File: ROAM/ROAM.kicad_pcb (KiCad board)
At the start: 4 copper layers, 90 x 56.8 mm, 11 parts, among them J1 CommanderX16Expansion Alt, U1 SST39SF040 (ROM), U2 74HCT00, U3 74HCT138, U4 AS6C4008 (RAM)

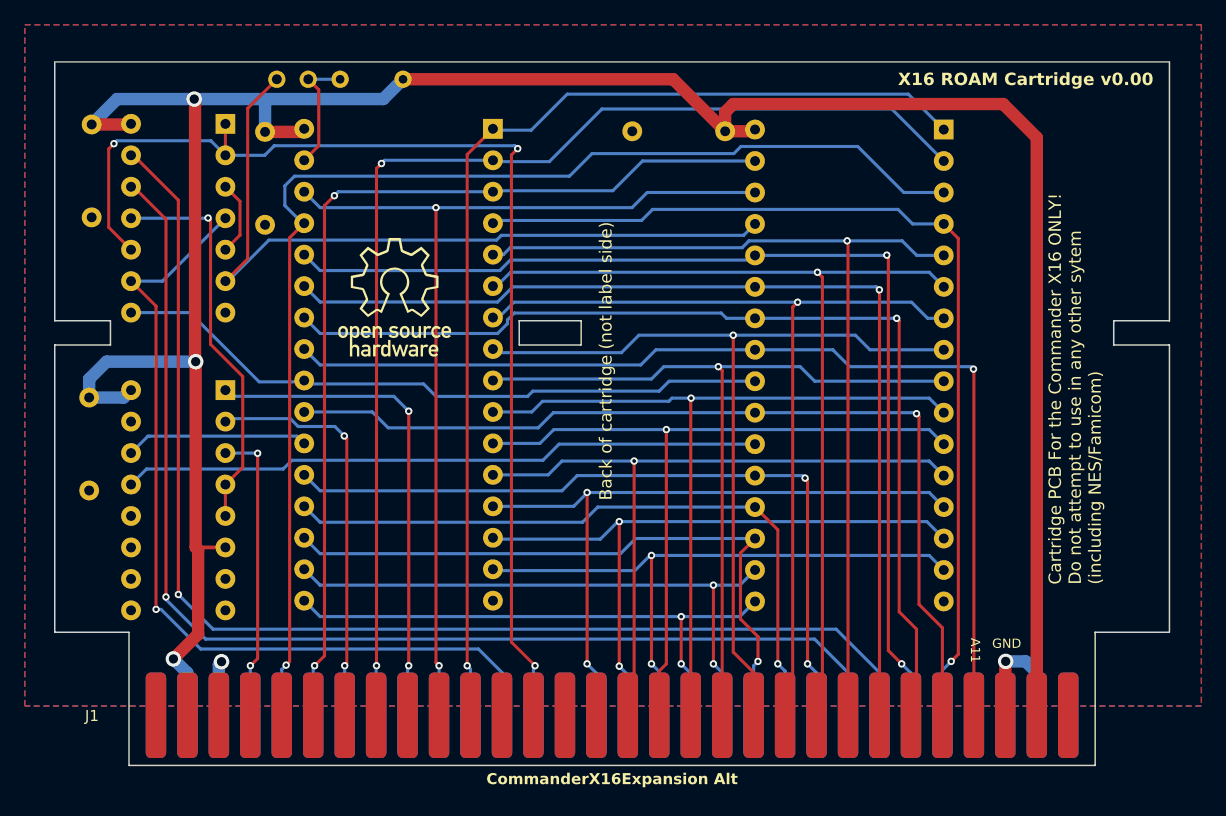
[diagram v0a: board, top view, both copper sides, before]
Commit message: Add NVRAM, add edge connector sym/fp to proj
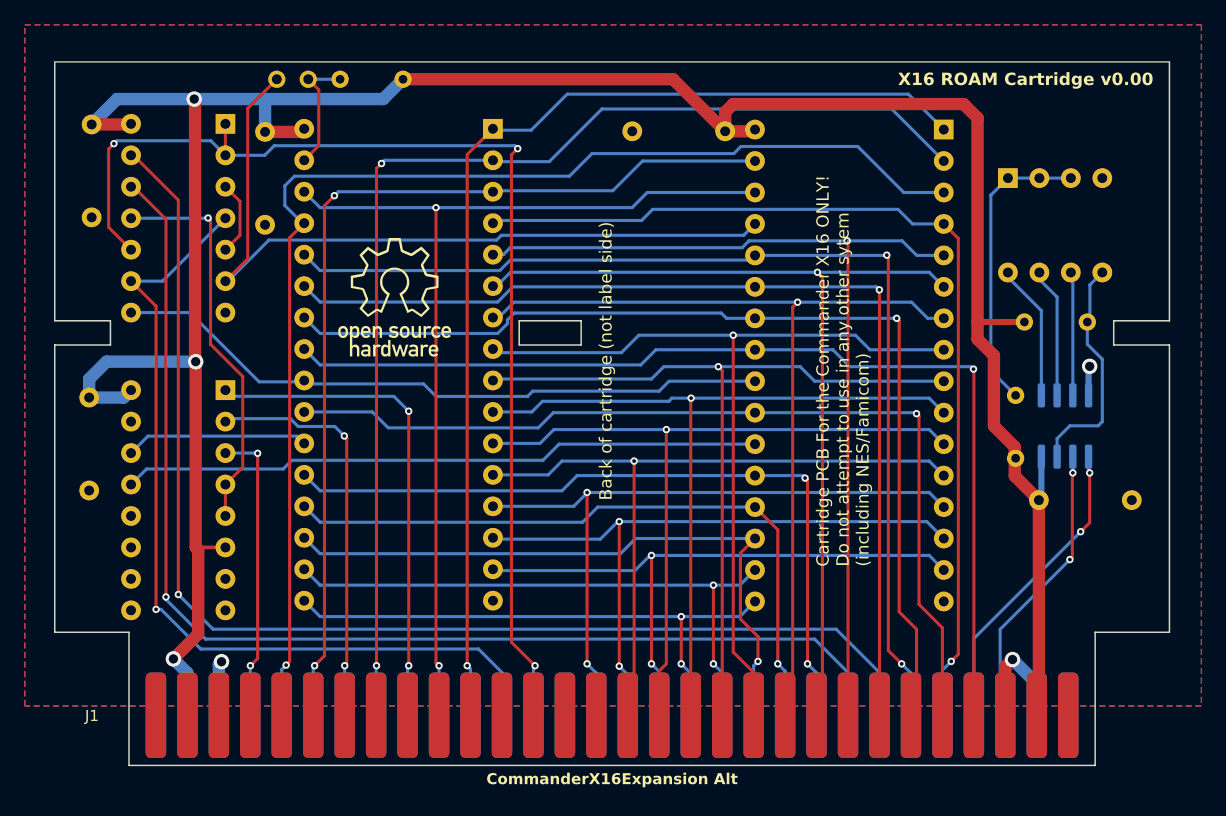
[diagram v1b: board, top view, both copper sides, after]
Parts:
- added C5: 100nF, Capacitor_THT:C_Axial_L3.8mm_D2.6mm_P7.50mm_Horizontal, B.Cu at (134.4, 113.4)
- added R2: 100K, Resistor_THT:R_Axial_DIN0204_L3.6mm_D1.6mm_P5.08mm_Horizontal, B.Cu at (125.0, 110.0)
- added R3: 100K, Resistor_THT:R_Axial_DIN0204_L3.6mm_D1.6mm_P5.08mm_Horizontal, B.Cu at (130.8, 99.0)
- added SW1: SW_DIP_x04, Button_Switch_THT:SW_DIP_SPSTx04_Slide_9.78x12.34mm_W7.62mm_P2.54mm, B.Cu at (124.4, 87.4)
- added U5: FM24C64B, Package_SO:SOIC-8_3.9x4.9mm_P1.27mm, B.Cu at (129.0, 107.4)
- J1: footprint CommanderX16Expansion:CommanderX16Cartridge -> X16Expansion:CommanderX16Cartridge
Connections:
- J1 pad 54: unconnected-(J1-SDA-Pad54) -> /SDA
- J1 pad 56: unconnected-(J1-SCL-Pad56) -> /SCL
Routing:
- net /SDA: track 0.00 -> 24.8 mm, vias 0 -> 2
- net Net-(R2-Pad2): track 0.00 -> 24.0 mm
- net /SCL: track 0.00 -> 22.9 mm, vias 0 -> 2
- net /WP: track 0.00 -> 18.4 mm
- net /FA0: track 0.00 -> 10.7 mm
- net /FA1: track 0.00 -> 9.95 mm
- net /FA2: track 0.00 -> 9.76 mm
- net +5V: track 208.5 -> 213.7 mm
- net GND: track 15.1 -> 14.3 mm, vias 2 -> 3
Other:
- board text added: "A0"
- board text added: "A1"
- board text added: "A2"
- board text added: "NVRAM Addr"
- board text added: "NVRAM Wr. Prot."
- board text removed: "A11"
- board text removed: "GND"
- board text removed: "SCL"

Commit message: Add jumpers to swap RAM/ROM
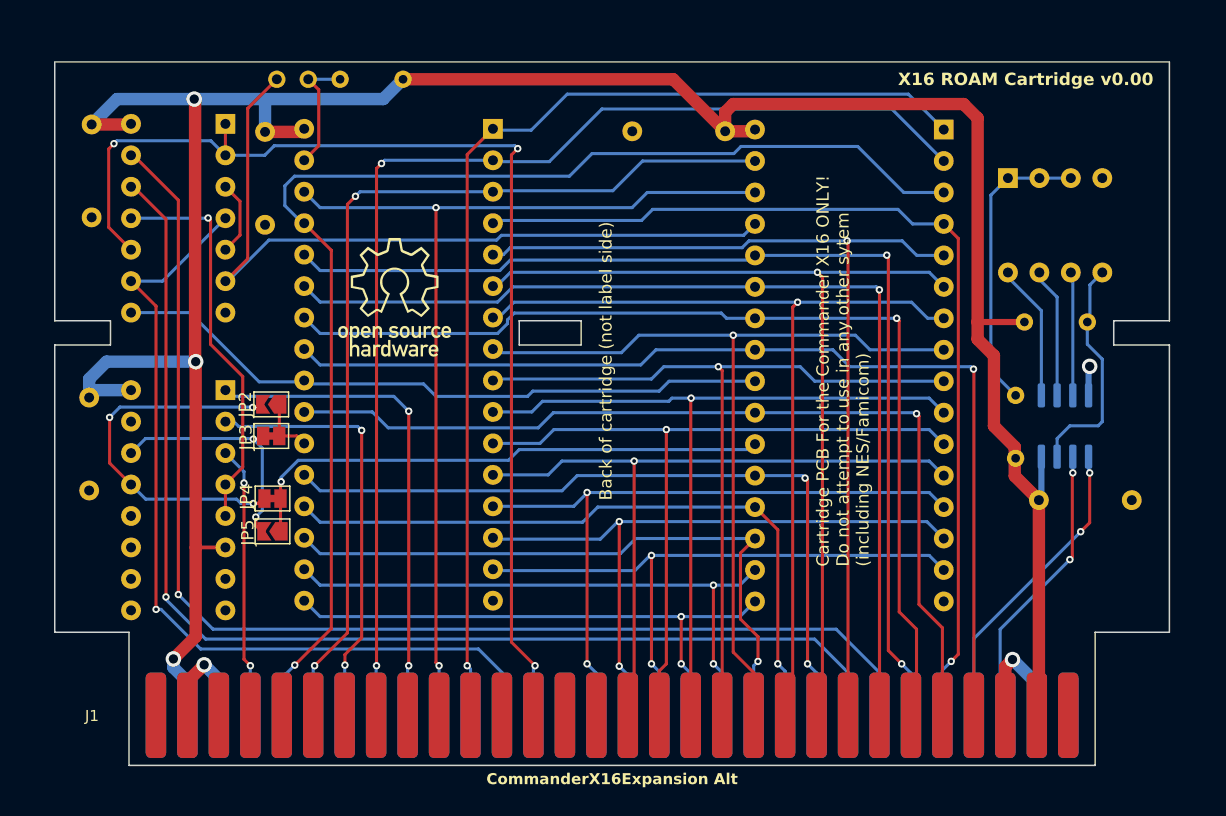
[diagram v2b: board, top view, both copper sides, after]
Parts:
- added JP2: BANK64_ROM, Jumper:SolderJumper-2_P1.3mm_Open_TrianglePad1.0x1.5mm, F.Cu at (64.9, 105.7)
- added JP3: BANK32_ROM, Jumper:SolderJumper-2_P1.3mm_Bridged_Pad1.0x1.5mm, F.Cu at (64.9, 108.2)
- added JP4: BANK64_RAM, Jumper:SolderJumper-2_P1.3mm_Bridged_Pad1.0x1.5mm, F.Cu at (65.0, 113.2)
- added JP5: BANK32_RAM, Jumper:SolderJumper-2_P1.3mm_Open_TrianglePad1.0x1.5mm, F.Cu at (65.0, 115.9)
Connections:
- U3 pad 13: !RAMBEN -> Net-(JP2-B)
- U3 pad 14: !ROMBEN -> Net-(JP3-A)
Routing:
- net Net-(JP2-B): track 0.00 -> 30.4 mm, vias 0 -> 3
- net Net-(JP3-A): track 0.00 -> 19.7 mm, vias 0 -> 2
- net !ROMBEN: track 14.8 -> 4.84 mm
- net !RAMBEN: track 51.7 -> 43.1 mm, vias 0 -> 1
- net +5V: track 213.7 -> 210.8 mm
- net /ROMB6: track 32.4 -> 34.5 mm
- net /ROMB7: track 24.0 -> 22.0 mm
- net ROMB0: track 100.1 -> 99.0 mm
- net ROMB1: track 77.7 -> 76.6 mm
- net GND: track 14.3 -> 13.5 mm
- removed copper zone on B.Cu, net GND
- removed copper zone on F.Cu, net GND

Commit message: Rounded connector edges; switched caps; NVRAM addr solder jumpers
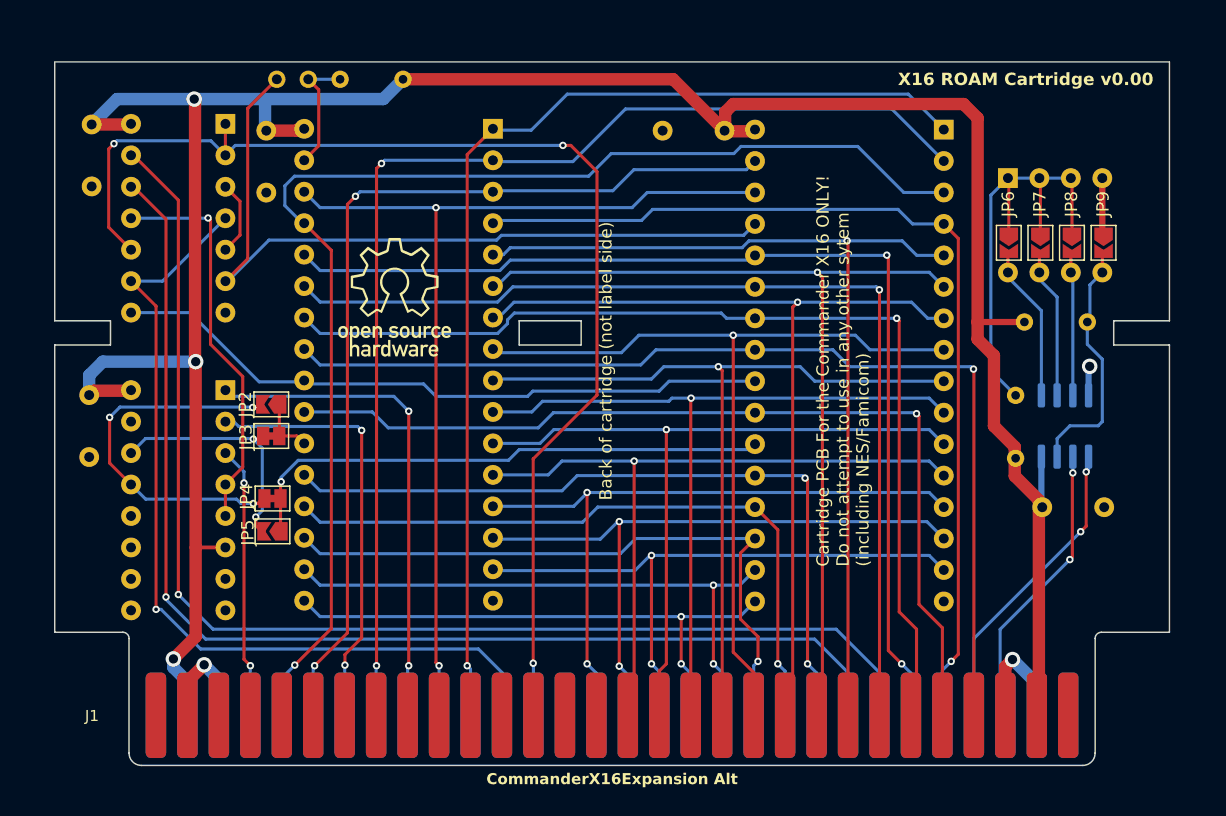
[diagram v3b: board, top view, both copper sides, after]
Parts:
- added JP6: JPFA0, Jumper:SolderJumper-2_P1.3mm_Open_TrianglePad1.0x1.5mm, F.Cu at (124.5, 92.6)
- added JP7: JPFA1, Jumper:SolderJumper-2_P1.3mm_Open_TrianglePad1.0x1.5mm, F.Cu at (127.0, 92.6)
- added JP8: JPFA2, Jumper:SolderJumper-2_P1.3mm_Open_TrianglePad1.0x1.5mm, F.Cu at (129.6, 92.6)
- added JP9: JPWP, Jumper:SolderJumper-2_P1.3mm_Open_TrianglePad1.0x1.5mm, F.Cu at (132.1, 92.6)
- C1, C2, C3, C4, C5: footprint Capacitor_THT:C_Axial_L3.8mm_D2.6mm_P7.50mm_Horizontal -> Capacitor_THT:C_Disc_D4.3mm_W1.9mm_P5.00mm
- moved C2 2.70 mm to (50.2, 109.9)
- moved C1 2.60 mm to (64.5, 88.5)
- moved C4 2.45 mm to (96.5, 83.5)
- moved C5 2.30 mm to (132.2, 114.0)
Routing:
- net Net-(JP6-A): track 24.0 -> 37.3 mm
- net /RWB: track 92.4 -> 98.9 mm
- net GND: track 13.5 -> 17.9 mm
- net /FA0: track 10.7 -> 12.3 mm
- net /FA1: track 9.95 -> 11.5 mm
- net /FA2: track 9.76 -> 11.3 mm
- net /WP: track 18.4 -> 20.0 mm
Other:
- outline, holes or cut-outs redrawn

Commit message: Cleaned up NVRAM Addr text
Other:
- board text added: "1"
- board text added: "2"
- board text added: "4"
- board text added: "NVRAM Addr 0x50 +"
- board text removed: "A0"
- board text removed: "A1"
- board text removed: "A2"
- board text removed: "NVRAM Addr"
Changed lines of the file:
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@@
 	)
 	(footprint "Button_Switch_THT:SW_DIP_SPSTx04_Slide_9.78x12.34mm_W7.62mm_P2.54mm"
+		(locked yes)
 		(layer "B.Cu")
 		(at 124.38 87.38 -90)
@@
 		)
 		(fp_text user "${REFERENCE}"
-			(at 7.27 -3.81 180)
+			(at 7.27 -3.81 360)
 			(layer "B.Fab")
 			(effects
@@
 	(gr_line
 		(start 130.88 85.58)
-		(end 130.88 80.58)
+		(end 130.88 79.15)
 		(stroke
 			(width 0.1)
@@
 		)
 	)
-	(gr_text "A0"
-		(at 124.48 85.78 90)
+	(gr_text "1"
+		(at 124.38 85.05 0)
 		(layer "B.SilkS")
 		(effects
@@
 				(thickness 0.2)
 			)
-			(justify right mirror)
+			(justify mirror)
 		)
 	)
@@
 		)
 	)
-	(gr_text "NVRAM Addr"
-		(at 130.48 82.18 0)
+	(gr_text "NVRAM Addr\n0x50 +"
+		(at 130.3 83.35 0)
 		(layer "B.SilkS")
 		(effects
@@
 		)
 	)
-	(gr_text "A1"
-		(at 127.08 85.78 90)
+	(gr_text "2"
+		(at 126.92 85.05 0)
 		(layer "B.SilkS")
 		(effects
@@
 				(thickness 0.2)
 			)
-			(justify right mirror)
+			(justify mirror)
 		)
 	)
-	(gr_text "A2"
-		(at 129.68 85.78 90)
+	(gr_text "4"
+		(at 128.682238 85.05 0)
 		(layer "B.SilkS")
 		(effects
